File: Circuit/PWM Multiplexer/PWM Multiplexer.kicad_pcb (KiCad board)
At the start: 2 copper layers, 63 parts, among them Q1 S8050, Q10 S8050, Q11 S8050, Q12 S8050, Q13 S8050, Q14 S8050, Q2 S8050, Q3 S8050, Q4 S8050, Q5 S8050, Q6 S8050, Q7 S8050, Q8 S8050, Q9 S8050, U1 74HC137, U2 74HC137, U3 L7805

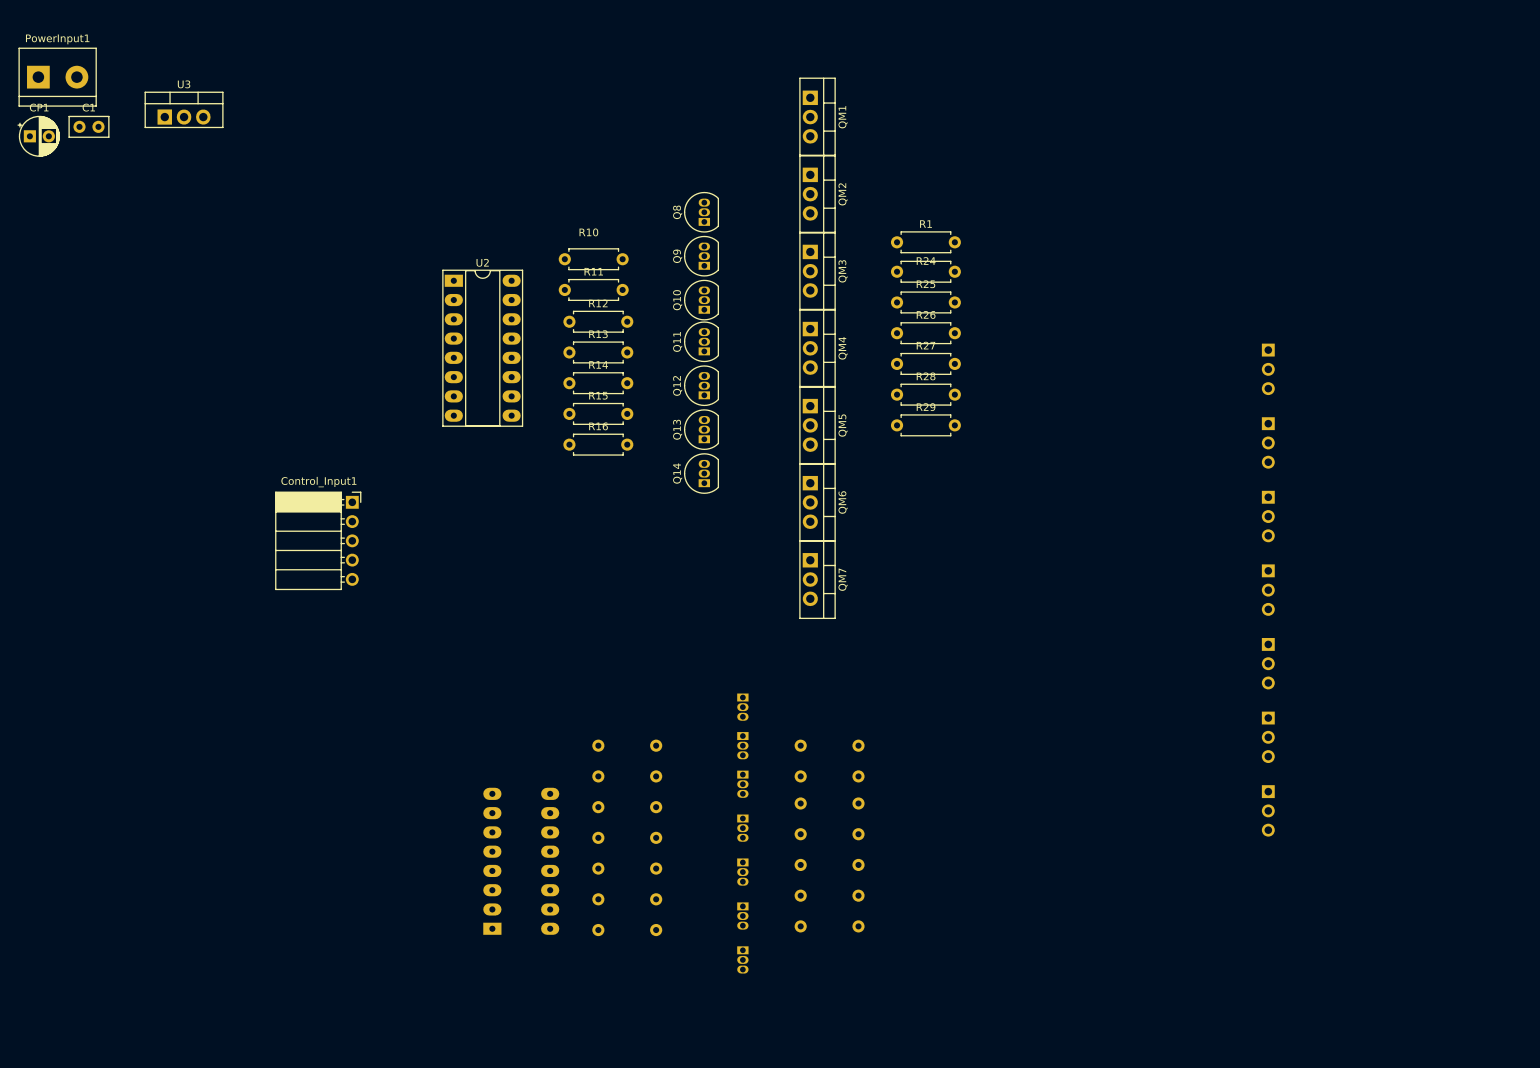
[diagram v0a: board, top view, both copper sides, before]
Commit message: PWM multiplexer circuit PCB traces ALL connected in a preliminary manner
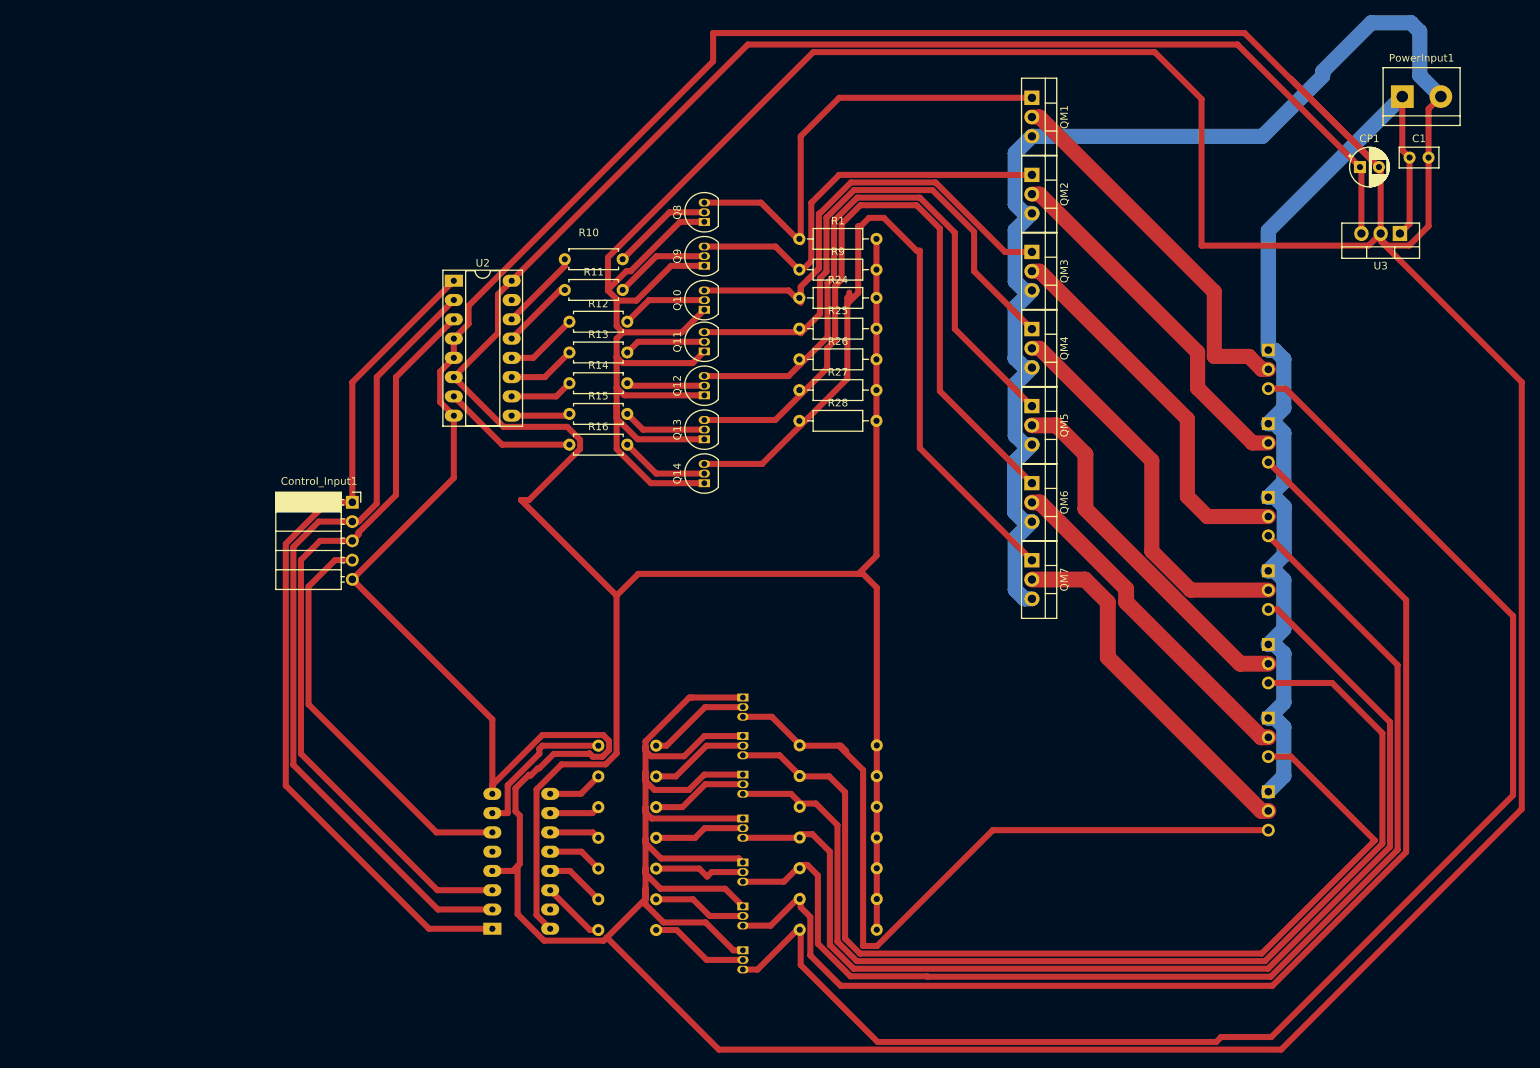
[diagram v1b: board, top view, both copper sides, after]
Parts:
- removed R29: 470, Resistor_THT:R_Axial_DIN0207_L6.3mm_D2.5mm_P7.62mm_Horizontal
- added R9: 470, Resistor_THT:R_Axial_DIN0207_L6.3mm_D2.5mm_P10.16mm_Horizontal, F.Cu at (139.5, 58.2)
- R1, R17, R18, R19, R20, R21, R22, R23, R24, R25, R26, R27, R28: footprint Resistor_THT:R_Axial_DIN0207_L6.3mm_D2.5mm_P7.62mm_Horizontal -> Resistor_THT:R_Axial_DIN0207_L6.3mm_D2.5mm_P10.16mm_Horizontal
- moved PowerInput1 179.8 mm to (219.0, 35.4)
- moved C1 175.4 mm to (220.0, 43.4)
- moved CP1 175.4 mm to (213.4, 44.7)
- moved U3 163.5 mm to (218.7, 53.5), turned to 180 degrees
- moved QM1 29.2 mm to (170.2, 35.6)
- moved QM2 29.2 mm to (170.2, 45.7)
- moved QM3 29.2 mm to (170.2, 55.9)
- moved QM4 29.2 mm to (170.2, 66.0)
- moved QM5 29.2 mm to (170.2, 76.2)
- moved QM6 29.2 mm to (170.2, 86.4)
- moved QM7 29.2 mm to (170.2, 96.5)
- moved R24 13.3 mm to (139.5, 61.9)
- moved R25 13.3 mm to (139.5, 66.0)
- moved R26 13.3 mm to (139.5, 70.0)
- moved R27 13.3 mm to (139.5, 74.1)
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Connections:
- R24 pad 1: Net-(Q9-C) -> Net-(Q10-C)
- R25 pad 1: Net-(Q10-C) -> Net-(Q11-C)
- R26 pad 1: Net-(Q11-C) -> Net-(Q12-C)
- R27 pad 1: Net-(Q12-C) -> Net-(Q13-C)
- R28 pad 1: Net-(Q13-C) -> Net-(Q14-C)
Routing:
- net GND: track 0.00 -> 1115.6 mm
- net +5V: track 0.00 -> 384.7 mm
- net D1_PWM: track 0.00 -> 194.9 mm
- net D2_PWM: track 0.00 -> 164.1 mm
- net D3_PWM: track 0.00 -> 154.0 mm
- net D4_PWM: track 0.00 -> 145.3 mm
- net D5_PWM: track 0.00 -> 141.2 mm
- net +12V: track 0.00 -> 131.1 mm
- net D6_PWM: track 0.00 -> 130.2 mm
- net A0: track 0.00 -> 112.7 mm
- net A1: track 0.00 -> 107.3 mm
- net Net-(Q14-C): track 0.00 -> 103.1 mm
- net D7_PWM: track 0.00 -> 103.0 mm
- net A2: track 0.00 -> 100.8 mm
- net Net-(Q13-C): track 0.00 -> 92.7 mm
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
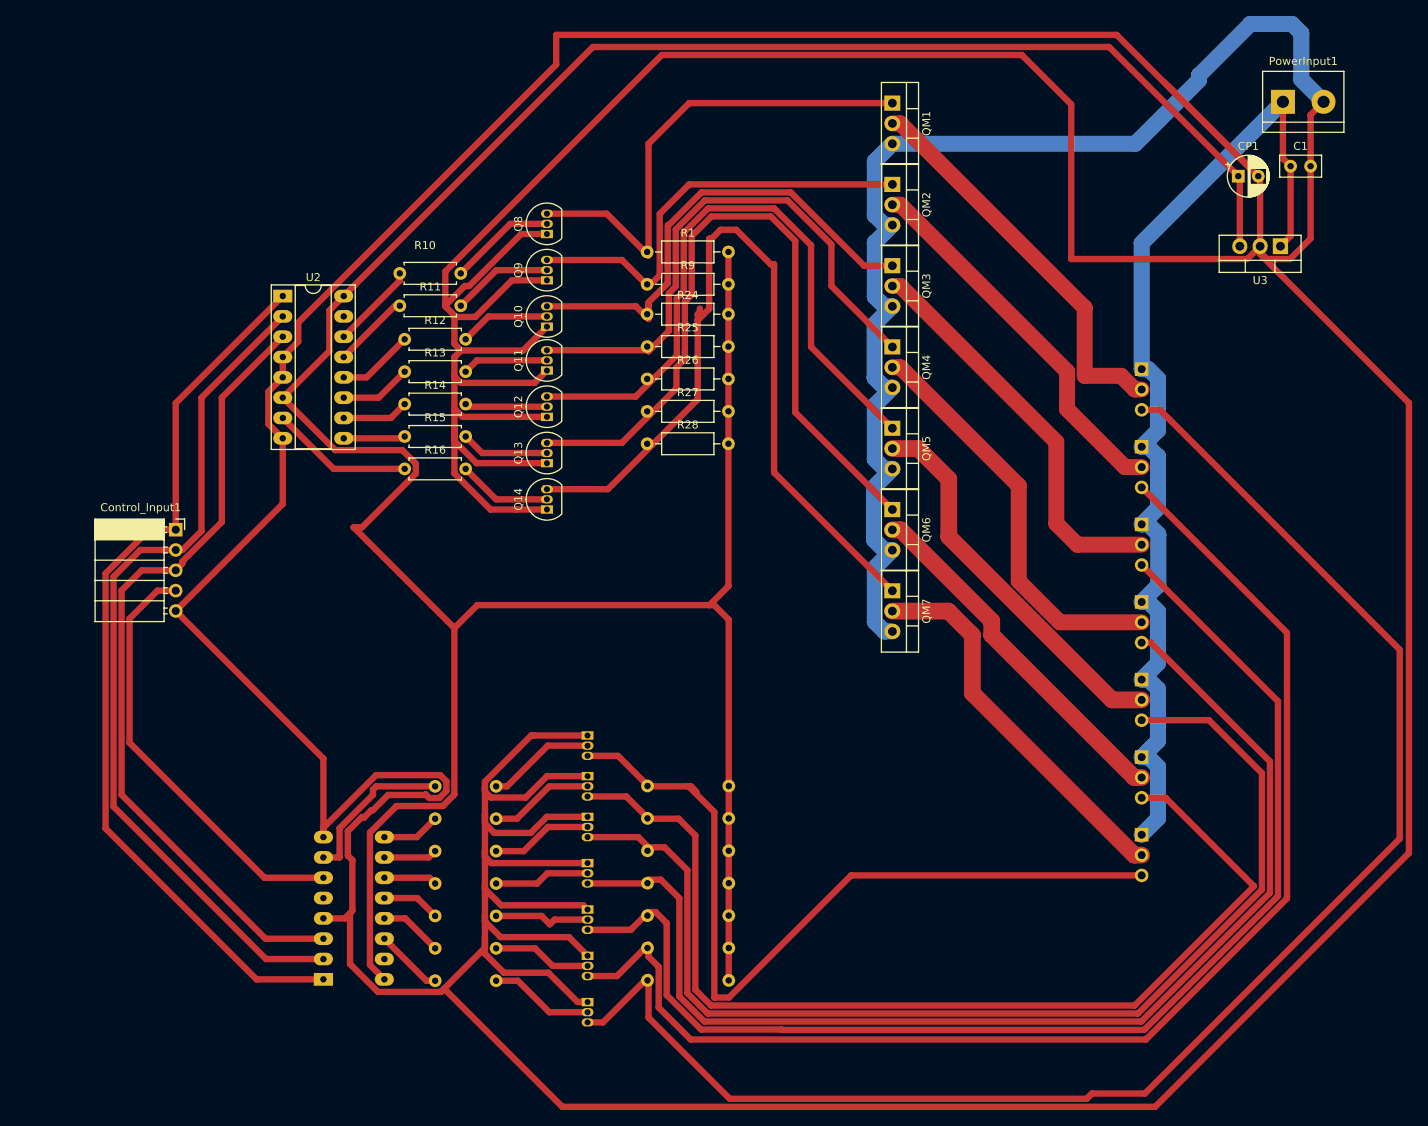
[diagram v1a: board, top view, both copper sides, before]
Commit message: Further development in PWM Multiplexer circuit PCB final design
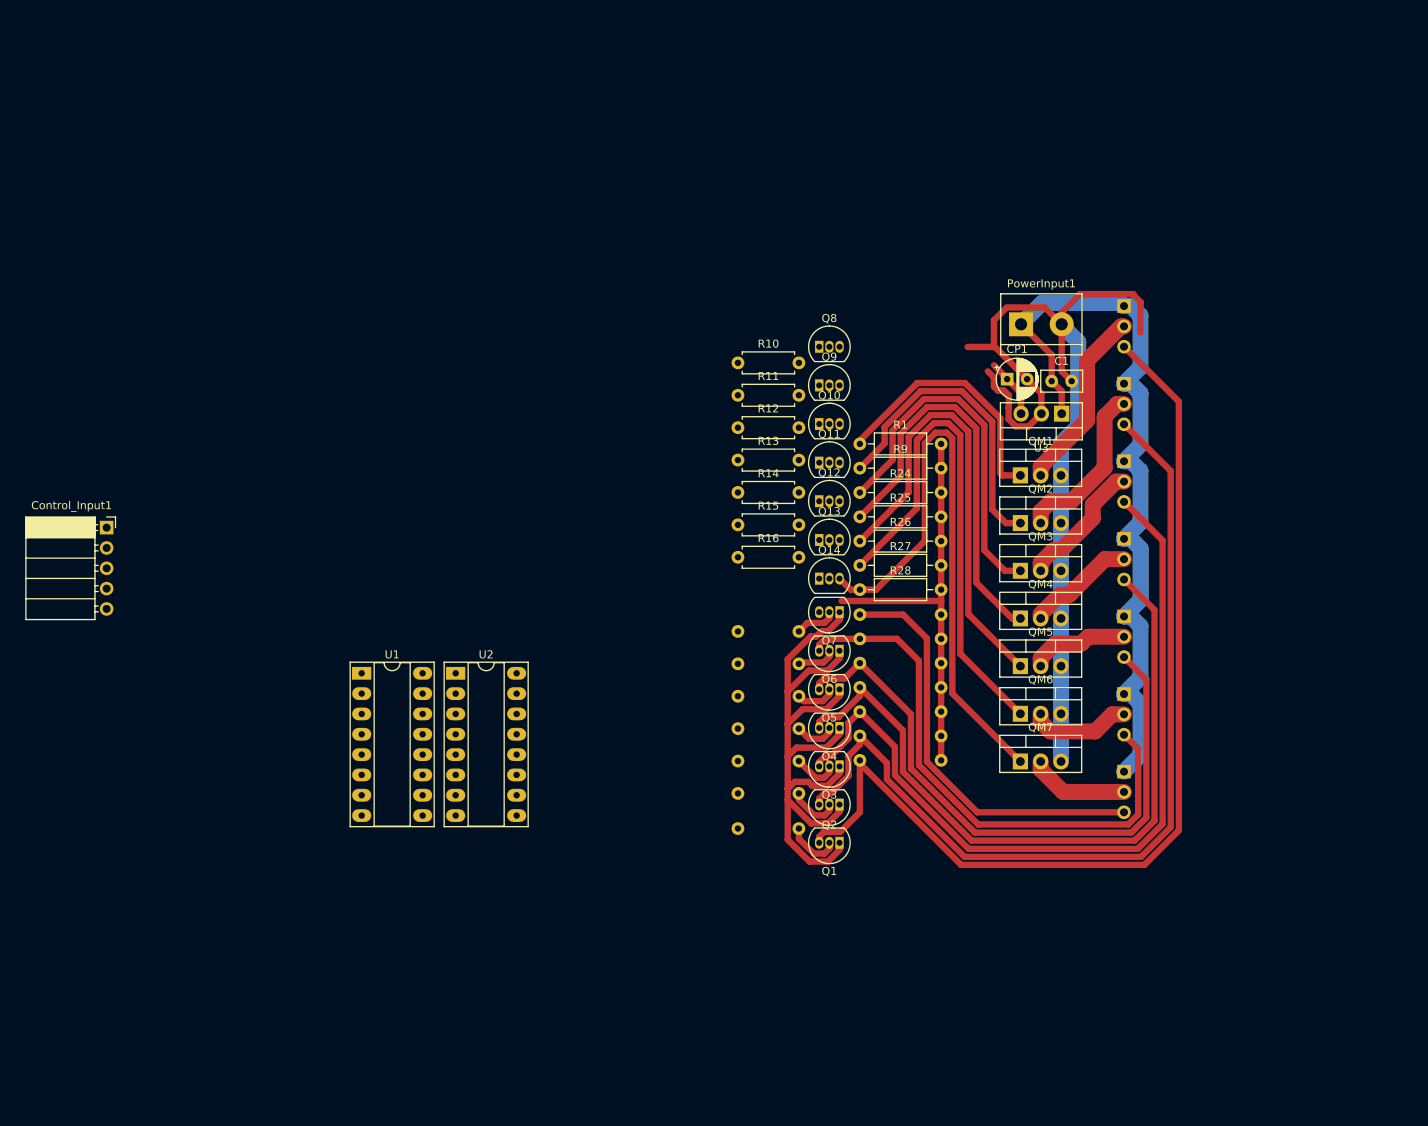
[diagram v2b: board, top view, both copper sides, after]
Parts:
- Q1, Q2, Q3, Q4, Q5, Q6, Q7, U1: moved to F.Cu
- moved U2 51.9 mm to (115.6, 106.8)
- moved QM1 49.2 mm to (186.2, 82.1), turned to 0 degrees
- moved QM2 45.3 mm to (186.2, 88.1), turned to 0 degrees
- moved R10 43.7 mm to (150.9, 68.0)
- moved R11 43.7 mm to (150.9, 72.1)
- moved R12 43.1 mm to (150.9, 76.1)
- moved R13 43.1 mm to (150.9, 80.2)
- moved R14 43.1 mm to (150.9, 84.2)
- moved R15 43.1 mm to (150.9, 88.3)
- moved R16 43.1 mm to (150.9, 92.3)
- moved PowerInput1 42.9 mm to (186.3, 63.2)
- moved R3 42.5 mm to (150.9, 121.8)
- moved R5 42.5 mm to (150.9, 113.8)
- moved R4 42.5 mm to (150.9, 117.8)
- moved R6 42.5 mm to (150.9, 109.7)
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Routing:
- net GND: track 1115.6 -> 205.8 mm
- net +5V: track 384.7 -> 59.5 mm
- net A0: track 112.7 -> 0.00 mm
- net A1: track 107.3 -> 0.00 mm
- net A2: track 100.8 -> 0.00 mm
- net D1_PWM: track 194.9 -> 124.2 mm
- net D5_PWM: track 141.2 -> 77.4 mm
- net D6_PWM: track 130.2 -> 69.4 mm
- net D4_PWM: track 145.3 -> 88.8 mm
- net D3_PWM: track 154.0 -> 99.9 mm
- net PWM: track 54.0 -> 0.00 mm
- net D2_PWM: track 164.1 -> 111.8 mm
- net D7_PWM: track 103.0 -> 52.3 mm
- net D4_Power: track 51.4 -> 13.8 mm
- net D5_Power: track 48.6 -> 12.5 mm
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
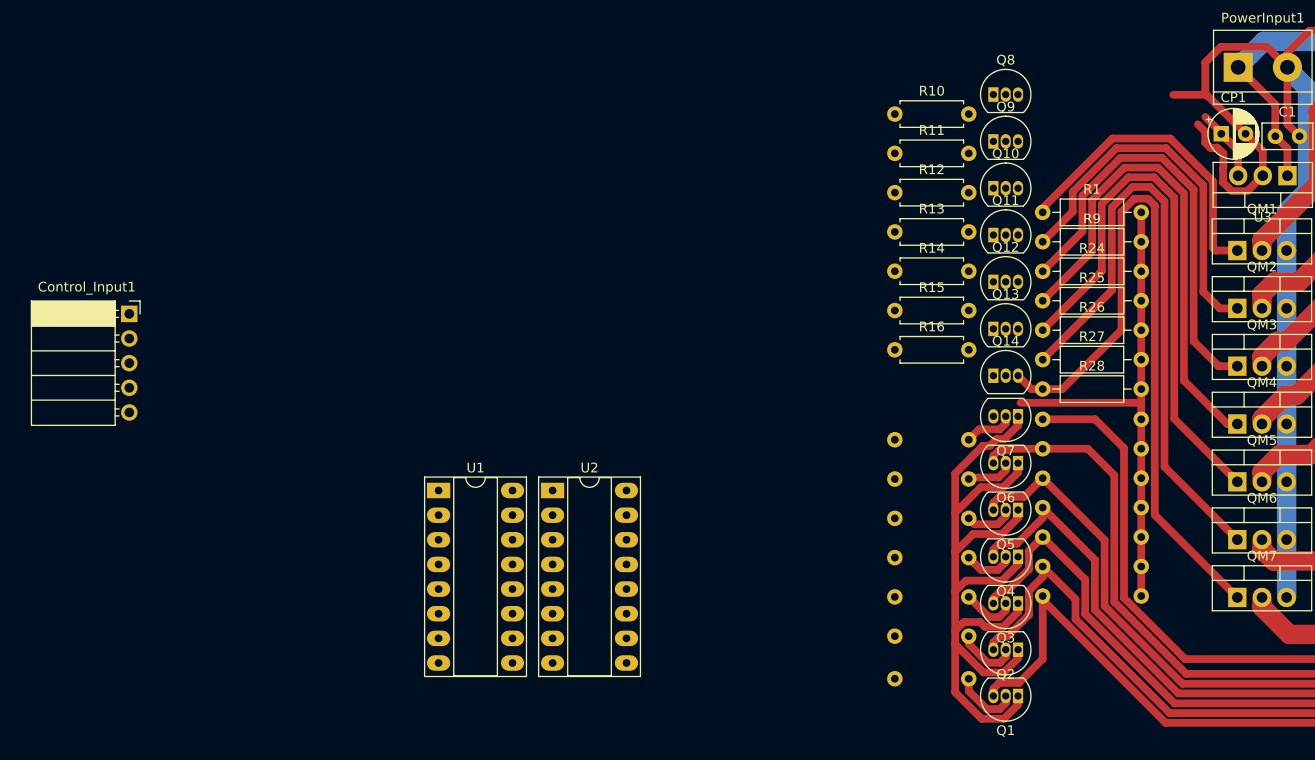
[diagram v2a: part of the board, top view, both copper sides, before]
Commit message: Fixed DC Motor Circuit and discovered fatal design flaw in PWM demultiplexer
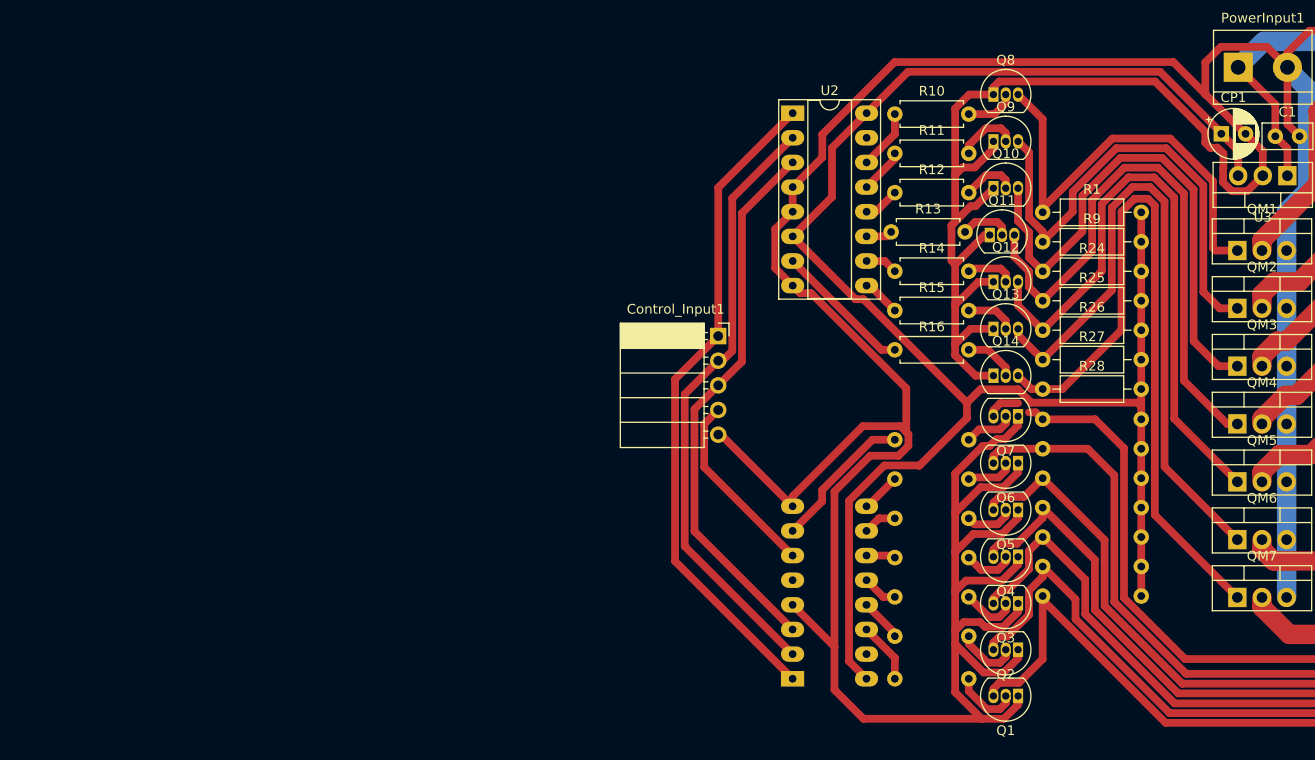
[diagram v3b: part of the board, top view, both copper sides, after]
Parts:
- U1: moved to B.Cu
- moved Control_Input1 60.7 mm to (132.7, 90.9)
- moved U2 46.1 mm to (140.3, 67.9)
- moved U1 41.3 mm to (140.3, 126.2)
- moved Q11 0.38 mm to (160.7, 80.5)
- moved R13 0.38 mm to (150.5, 80.2)
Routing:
- net GND: track 205.8 -> 453.6 mm
- net +5V: track 59.5 -> 182.2 mm
- net A0: track 0.00 -> 68.3 mm
- net A1: track 0.00 -> 62.7 mm
- net A2: track 0.00 -> 56.5 mm
- net PWM: track 0.00 -> 19.4 mm
- net Net-(U1-~{Y7}): track 0.00 -> 15.1 mm
- net Net-(U2-~{Y7}): track 0.00 -> 14.3 mm
- net Net-(Q8-C): track 32.3 -> 45.5 mm
- net Net-(Q9-C): track 38.5 -> 49.9 mm
- net Net-(Q10-C): track 45.1 -> 54.7 mm
- net Net-(Q11-C): track 51.1 -> 59.1 mm
- net Net-(Q9-B): track 0.00 -> 6.43 mm
- net Net-(U1-~{Y1}): track 0.00 -> 6.29 mm
- net Net-(U2-~{Y1}): track 0.00 -> 6.19 mm
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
